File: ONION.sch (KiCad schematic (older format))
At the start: 11 parts

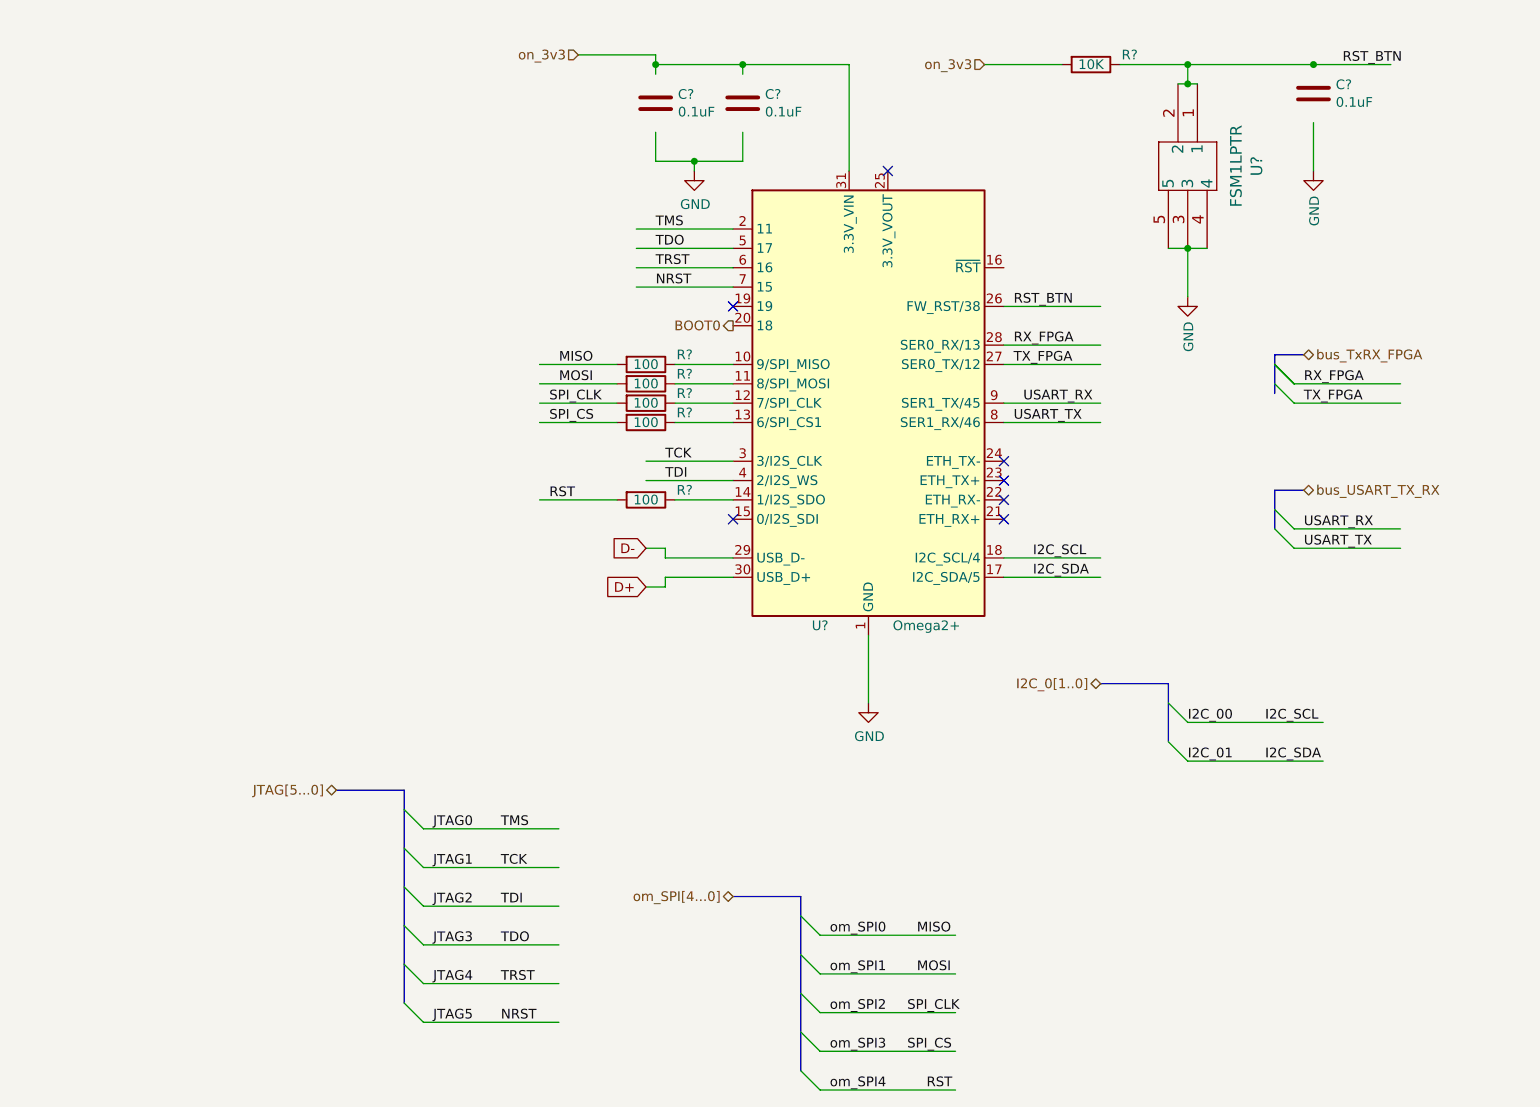
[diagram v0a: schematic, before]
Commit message: asignacion pines de control
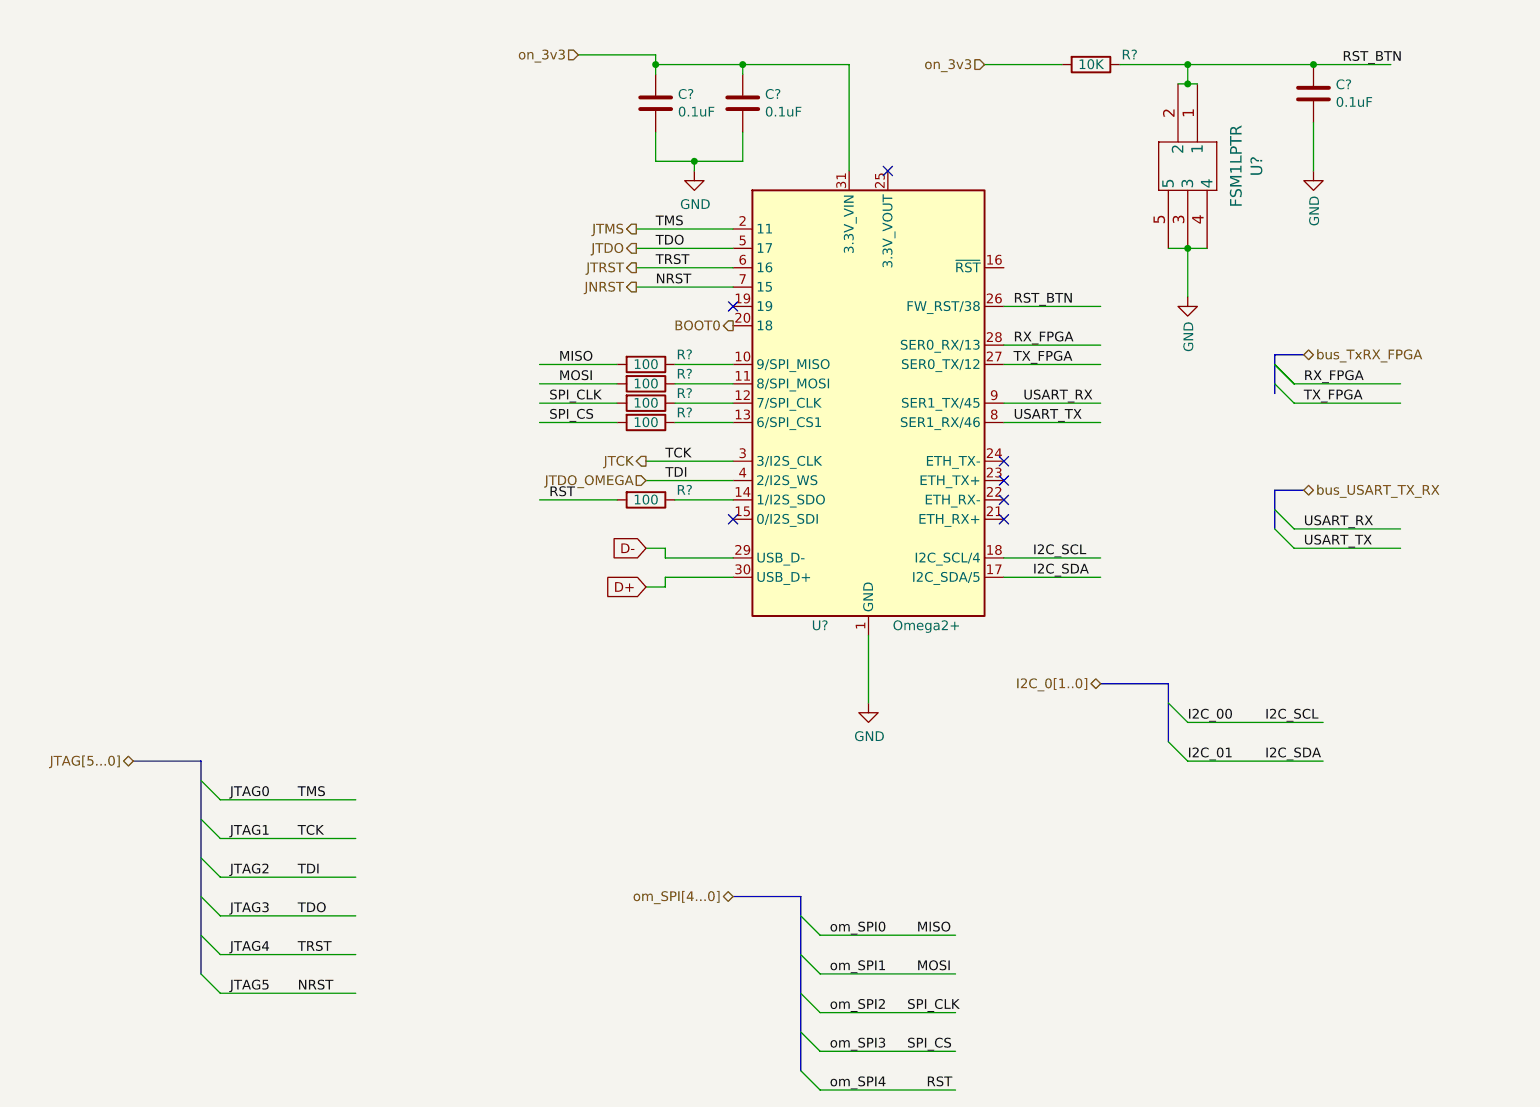
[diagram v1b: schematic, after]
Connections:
- net labels added: JNRST, JTCK, JTDO, JTDO_OMEGA, JTMS, JTRST
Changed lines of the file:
@@
 $Descr A4 11693 8268
 encoding utf-8
-Sheet 4 5
+Sheet 4 6
 Title ""
 Date ""
@@
 $Comp
 L Device:C C?
-U 0 1 5D451473
+U 1 1 5D451473
 P 4350 1700
 AR Path="/5CD05F2F/5D451473" Ref="C?"  Part="0"
@@
 F 2 "Capacitor_SMD:C_0603_1608Metric_Pad1.05x0.95mm_HandSolder" H 4388 1550 50  0001 C CNN
 F 3 "" H 4350 1700 50  0001 C CNN
-	0    4350 1700
+	1    4350 1700
 	1    0    0    -1
 $EndComp
@@
 $Comp
 L Device:C C?
-U 0 1 5D44FAD3
+U 1 1 5D44FAD3
 P 3900 1700
 AR Path="/5CD05F2F/5D44FAD3" Ref="C?"  Part="0"
@@
 F 2 "Capacitor_SMD:C_0603_1608Metric_Pad1.05x0.95mm_HandSolder" H 3938 1550 50  0001 C CNN
 F 3 "" H 3900 1700 50  0001 C CNN
-	0    3900 1700
+	1    3900 1700
 	1    0    0    -1
 $EndComp
@@
 USART_TX
 Wire Bus Line
-	2250 5250 2600 5250
-Entry Wire Line
-	2600 5350 2700 5450
-Entry Wire Line
-	2600 5550 2700 5650
-Entry Wire Line
-	2600 5750 2700 5850
-Entry Wire Line
-	2600 5950 2700 6050
-Entry Wire Line
-	2600 6150 2700 6250
-Entry Wire Line
-	2600 6350 2700 6450
-Wire Wire Line
-	2700 5450 3400 5450
-Wire Wire Line
-	2700 5650 3400 5650
-Wire Wire Line
-	2700 5850 3400 5850
-Wire Wire Line
-	2700 6050 3400 6050
-Wire Wire Line
-	2700 6250 3400 6250
-Wire Wire Line
-	2700 6450 3400 6450
-Wire Bus Line
 	6200 4700 6550 4700
 Entry Wire Line
@@
 Wire Wire Line
 	4750 6800 5450 6800
-Text Label 2750 5450 0    50   ~ 0
-JTAG0
-Text Label 2750 5650 0    50   ~ 0
-JTAG1
-Text Label 2750 5850 0    50   ~ 0
-JTAG2
-Text Label 2750 6050 0    50   ~ 0
-JTAG3
-Text Label 2750 6250 0    50   ~ 0
-JTAG4
-Text Label 2750 6450 0    50   ~ 0
-JTAG5
-Text HLabel 2250 5250 0    50   BiDi ~ 0
-JTAG[5...0]
-Text Label 3100 5450 0    50   ~ 0
-TMS
-Text Label 3100 5650 0    50   ~ 0
-TCK
-Text Label 3100 5850 0    50   ~ 0
-TDI
-Text Label 3100 6050 0    50   ~ 0
-TDO
-Text Label 3100 6250 0    50   ~ 0
-TRST
-Text Label 3100 6450 0    50   ~ 0
-NRST
 Wire Wire Line
 	4300 2350 3800 2350
@@
 Text Label 5300 6800 0    50   ~ 0
 RST
-Text HLabel 4300 5800 0    50   BiDi ~ 0
-om_SPI[4...0]
 $Comp
 L BAT2032:R R?
@@
 $Comp
 L Device:C C?
-U 0 1 5CD5AB36
+U 1 1 5CD5AB36
 P 7300 1650
 AR Path="/5CD05F2F/5CD5AB36" Ref="C?"  Part="0"
@@
 F 2 "Capacitor_SMD:C_0603_1608Metric_Pad1.05x0.95mm_HandSolder" H 7338 1500 50  0001 C CNN
 F 3 "" H 7300 1650 50  0001 C CNN
-	0    7300 1650
+	1    7300 1650
 	1    0    0    -1
 $EndComp
@@
 	0    1    1    0
 $EndComp
+Text HLabel 4300 5800 0    50   BiDi ~ 0
+om_SPI[4...0]
+Text Label 2050 6300 0    50   ~ 0
+NRST
+Text Label 2050 6100 0    50   ~ 0
+TRST
+Text Label 2050 5900 0    50   ~ 0
+TDO
+Text Label 2050 5700 0    50   ~ 0
+TDI
+Text Label 2050 5500 0    50   ~ 0
+TCK
+Text Label 2050 5300 0    50   ~ 0
+TMS
+Text HLabel 1200 5100 0    50   BiDi ~ 0
+JTAG[5...0]
+Text Label 1700 6300 0    50   ~ 0
+JTAG5
+Text Label 1700 6100 0    50   ~ 0
+JTAG4
+Text Label 1700 5900 0    50   ~ 0
+JTAG3
+Text Label 1700 5700 0    50   ~ 0
+JTAG2
+Text Label 1700 5500 0    50   ~ 0
+JTAG1
+Text Label 1700 5300 0    50   ~ 0
+JTAG0
+Wire Wire Line
+	1650 6300 2350 6300
+Wire Wire Line
+	1650 6100 2350 6100
+Wire Wire Line
+	1650 5900 2350 5900
+Wire Wire Line
+	1650 5700 2350 5700
+Wire Wire Line
+	1650 5500 2350 5500
+Wire Wire Line
+	1650 5300 2350 5300
+Entry Wire Line
+	1550 6200 1650 6300
+Entry Wire Line
+	1550 6000 1650 6100
+Entry Wire Line
+	1550 5800 1650 5900
+Entry Wire Line
+	1550 5600 1650 5700
+Entry Wire Line
+	1550 5400 1650 5500
+Entry Wire Line
+	1550 5200 1650 5300
+Wire Bus Line
+	1200 5100 1550 5100
+Text HLabel 3800 2450 0    50   Output ~ 0
+JTDO
+Text HLabel 3800 2350 0    50   Output ~ 0
+JTMS
+Text HLabel 3800 2550 0    50   Output ~ 0
+JTRST
+Text HLabel 3800 2650 0    50   Output ~ 0
+JNRST
+Text HLabel 3850 3550 0    50   Output ~ 0
+JTCK
+Text HLabel 3850 3650 0    50   Input ~ 0
+JTDO_OMEGA
 Wire Bus Line
 	6550 4700 6550 5000
@@
 	4650 5800 4650 6700
 Wire Bus Line
-	2600 5250 2600 6350
+	1550 5100 1550 6200
 $EndSCHEMATC

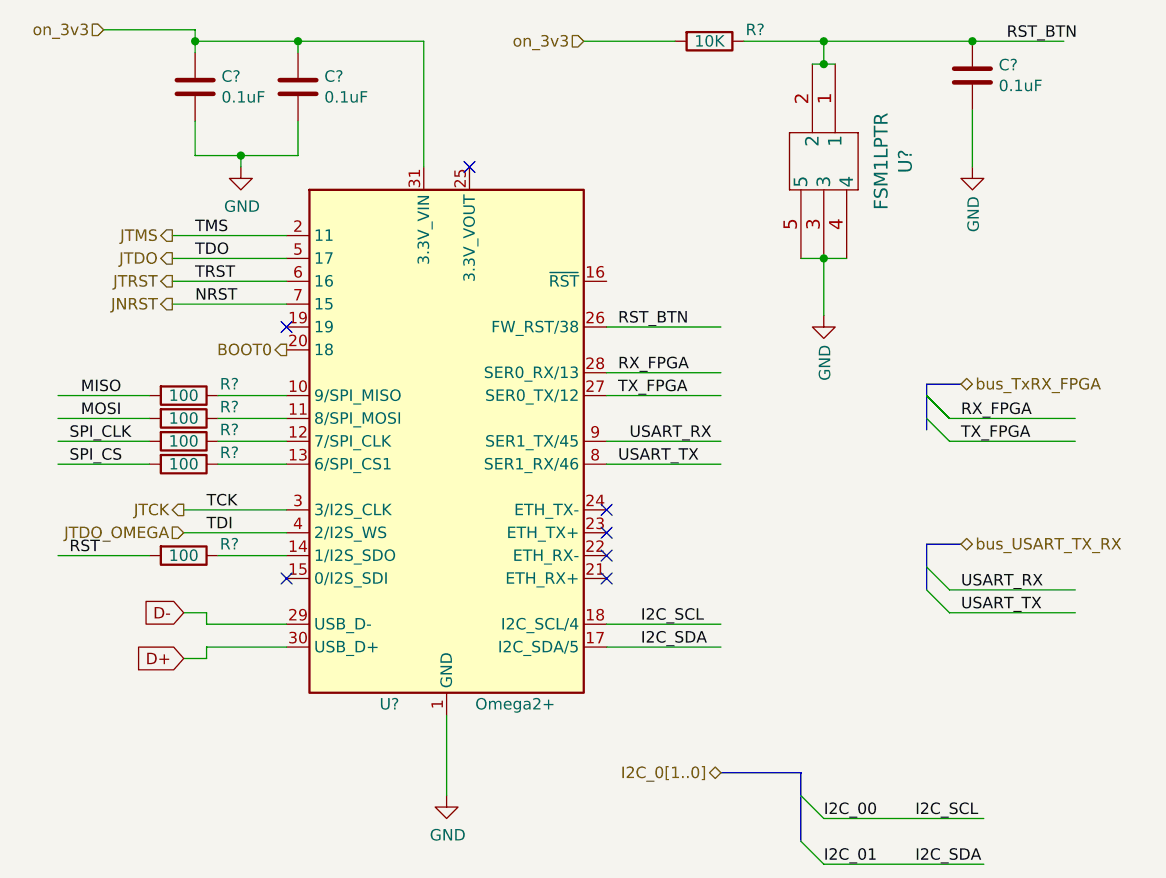
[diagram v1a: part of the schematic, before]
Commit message: asignacion pines de control
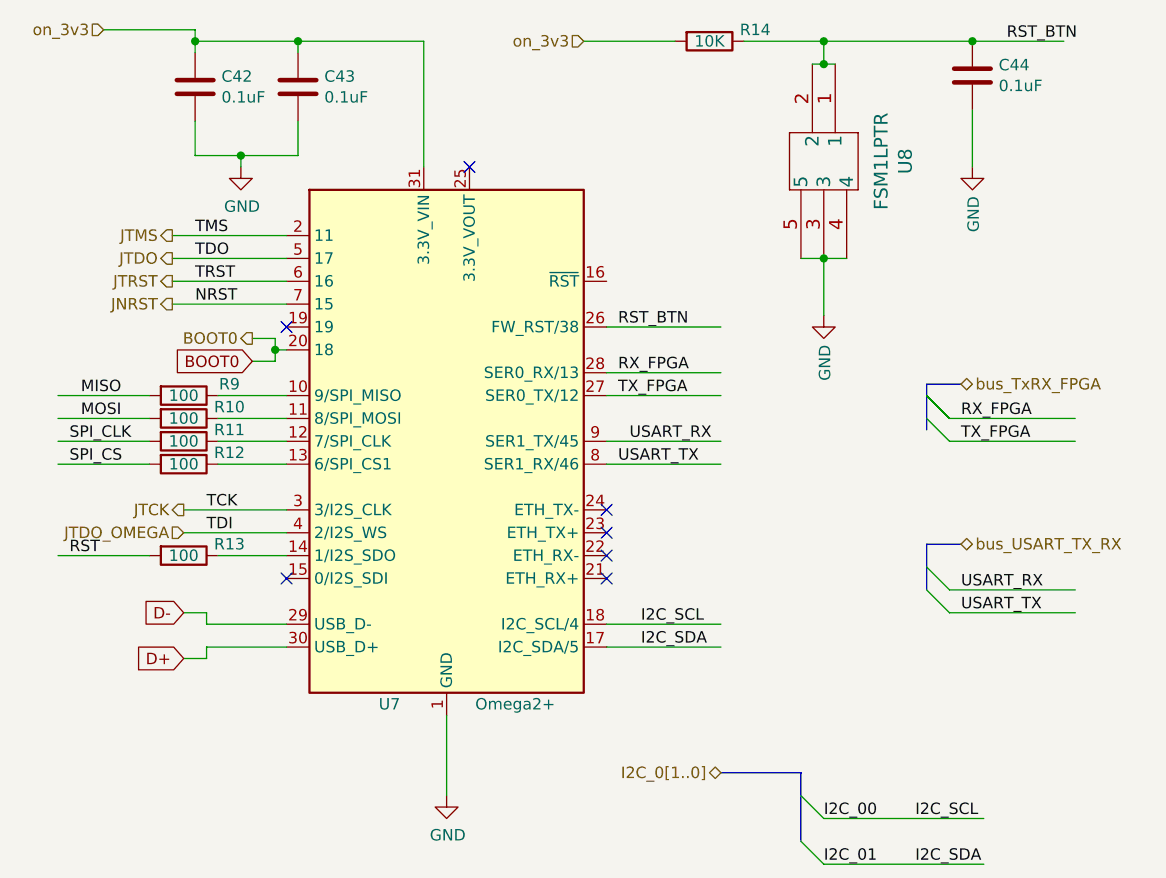
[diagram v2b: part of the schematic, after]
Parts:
- gave numbers to parts that had none: 11
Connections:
- wire segments 70 -> 75
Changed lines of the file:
@@
 $EndDescr
 $Comp
-L power:GND #PWR?
+L power:GND #PWR0143
 U 1 1 5D428107
 P 5000 4800
-F 0 "#PWR?" H 5000 4550 50  0001 C CNN
+F 0 "#PWR0143" H 5000 4550 50  0001 C CNN
 F 1 "GND" H 5005 4627 50  0000 C CNN
 F 2 "" H 5000 4800 50  0001 C CNN
@@
 P 4350 1700
 AR Path="/5CD05F2F/5D451473" Ref="C?"  Part="0"
-AR Path="/5D3DE78E/5D451473" Ref="C?"  Part="0"
-F 0 "C?" H 4465 1746 50  0000 L CNN
+AR Path="/5D3DE78E/5D451473" Ref="C43"  Part="1"
+F 0 "C43" H 4465 1746 50  0000 L CNN
 F 1 "0.1uF" H 4465 1655 50  0000 L CNN
 F 2 "Capacitor_SMD:C_0603_1608Metric_Pad1.05x0.95mm_HandSolder" H 4388 1550 50  0001 C CNN
@@
 	4350 2000 4100 2000
 $Comp
-L power:GND #PWR?
+L power:GND #PWR0144
 U 1 1 5D454107
 P 4100 2050
-F 0 "#PWR?" H 4100 1800 50  0001 C CNN
+F 0 "#PWR0144" H 4100 1800 50  0001 C CNN
 F 1 "GND" H 4105 1877 50  0000 C CNN
 F 2 "" H 4100 2050 50  0001 C CNN
@@
 P 3900 1700
 AR Path="/5CD05F2F/5D44FAD3" Ref="C?"  Part="0"
-AR Path="/5D3DE78E/5D44FAD3" Ref="C?"  Part="0"
-F 0 "C?" H 4015 1746 50  0000 L CNN
+AR Path="/5D3DE78E/5D44FAD3" Ref="C42"  Part="1"
+F 0 "C42" H 4015 1746 50  0000 L CNN
 F 1 "0.1uF" H 4015 1655 50  0000 L CNN
 F 2 "Capacitor_SMD:C_0603_1608Metric_Pad1.05x0.95mm_HandSolder" H 3938 1550 50  0001 C CNN
@@
 NoConn ~ 5700 3850
 $Comp
-L MCU_Module:Omega2+ U?
+L MCU_Module:Omega2+ U7
 U 1 1 5D3DE9E1
 P 5000 3250
-F 0 "U?" H 4750 2100 50  0000 C CNN
+F 0 "U7" H 4750 2100 50  0000 C CNN
 F 1 "Omega2+" H 5300 2100 50  0000 C CNN
 F 2 "Module:Onion_Omega2+" H 5000 1750 50  0001 C CNN
@@
 RST
 $Comp
-L BAT2032:R R?
+L BAT2032:R R9
 U 1 1 5CD91C3B
 P 3850 3050
-F 0 "R?" V 3800 3250 50  0000 C CNN
+F 0 "R9" V 3800 3250 50  0000 C CNN
 F 1 "100" V 3850 3050 50  0000 C CNN
 F 2 "Resistor_SMD:R_0603_1608Metric_Pad1.05x0.95mm_HandSolder" V 3780 3050 50  0001 C CNN
@@
 $EndComp
 $Comp
-L BAT2032:R R?
+L BAT2032:R R10
 U 1 1 5CD95E75
 P 3850 3150
-F 0 "R?" V 3800 3350 50  0000 C CNN
+F 0 "R10" V 3800 3350 50  0000 C CNN
 F 1 "100" V 3850 3150 50  0000 C CNN
 F 2 "Resistor_SMD:R_0603_1608Metric_Pad1.05x0.95mm_HandSolder" V 3780 3150 50  0001 C CNN
@@
 $EndComp
 $Comp
-L BAT2032:R R?
+L BAT2032:R R11
 U 1 1 5CD970C9
 P 3850 3250
-F 0 "R?" V 3800 3450 50  0000 C CNN
+F 0 "R11" V 3800 3450 50  0000 C CNN
 F 1 "100" V 3850 3250 50  0000 C CNN
 F 2 "Resistor_SMD:R_0603_1608Metric_Pad1.05x0.95mm_HandSolder" V 3780 3250 50  0001 C CNN
@@
 $EndComp
 $Comp
-L BAT2032:R R?
+L BAT2032:R R12
 U 1 1 5CD983F0
 P 3850 3350
-F 0 "R?" V 3800 3550 50  0000 C CNN
+F 0 "R12" V 3800 3550 50  0000 C CNN
 F 1 "100" V 3850 3350 50  0000 C CNN
 F 2 "Resistor_SMD:R_0603_1608Metric_Pad1.05x0.95mm_HandSolder" V 3780 3350 50  0001 C CNN
@@
 SPI_CS
 $Comp
-L BAT2032:R R?
+L BAT2032:R R13
 U 1 1 5CD3D226
 P 3850 3750
-F 0 "R?" V 3800 3950 50  0000 C CNN
+F 0 "R13" V 3800 3950 50  0000 C CNN
 F 1 "100" V 3850 3750 50  0000 C CNN
 F 2 "Resistor_SMD:R_0603_1608Metric_Pad1.05x0.95mm_HandSolder" V 3780 3750 50  0001 C CNN
@@
 Text Label 3350 3750 0    50   ~ 0
 RST
-Text HLabel 4300 2850 0    50   Output ~ 0
+Text HLabel 4150 2800 0    50   Output ~ 0
 BOOT0
 $Comp
-L power:GND #PWR?
+L power:GND #PWR0145
 U 1 1 5CD47976
 P 6650 2700
-F 0 "#PWR?" H 6650 2450 50  0001 C CNN
+F 0 "#PWR0145" H 6650 2450 50  0001 C CNN
 F 1 "GND" V 6655 2572 50  0000 R CNN
 F 2 "" H 6650 2700 50  0001 C CNN
@@
 	7300 2050 7300 1800
 $Comp
-L power:GND #PWR?
+L power:GND #PWR0146
 U 1 1 5CD5D462
 P 7300 2050
-F 0 "#PWR?" H 7300 1800 50  0001 C CNN
+F 0 "#PWR0146" H 7300 1800 50  0001 C CNN
 F 1 "GND" V 7305 1922 50  0000 R CNN
 F 2 "" H 7300 2050 50  0001 C CNN
@@
 P 7300 1650
 AR Path="/5CD05F2F/5CD5AB36" Ref="C?"  Part="0"
-AR Path="/5D3DE78E/5CD5AB36" Ref="C?"  Part="0"
-F 0 "C?" H 7415 1696 50  0000 L CNN
+AR Path="/5D3DE78E/5CD5AB36" Ref="C44"  Part="1"
+F 0 "C44" H 7415 1696 50  0000 L CNN
 F 1 "0.1uF" H 7415 1605 50  0000 L CNN
 F 2 "Capacitor_SMD:C_0603_1608Metric_Pad1.05x0.95mm_HandSolder" H 7338 1500 50  0001 C CNN
@@
 $EndComp
 $Comp
-L BAT2032:R R?
+L BAT2032:R R14
 U 1 1 5CD54029
 P 6150 1500
-F 0 "R?" V 6100 1700 50  0000 C CNN
+F 0 "R14" V 6100 1700 50  0000 C CNN
 F 1 "10K" V 6150 1500 50  0000 C CNN
 F 2 "Resistor_SMD:R_0603_1608Metric_Pad1.05x0.95mm_HandSolder" V 6080 1500 50  0001 C CNN
@@
 	6750 2450 6650 2450
 $Comp
-L FSM1LPTR:FSM1LPTR U?
+L FSM1LPTR:FSM1LPTR U8
 U 1 1 5D472323
 P 6700 2000
-F 0 "U?" H 6725 2307 60  0000 C CNN
+F 0 "U8" H 6725 2307 60  0000 C CNN
 F 1 "FSM1LPTR" H 6725 2201 60  0000 C CNN
 F 2 "SWITCH_FSM1LPA" H 6700 2150 60  0001 C CNN
@@
 Text HLabel 3850 3650 0    50   Input ~ 0
 JTDO_OMEGA
+Text GLabel 4150 2900 0    50   Input ~ 0
+BOOT0
+Wire Wire Line
+	4300 2850 4250 2850
+Wire Wire Line
+	4250 2850 4250 2800
+Wire Wire Line
+	4250 2800 4150 2800
+Wire Wire Line
+	4150 2900 4250 2900
+Wire Wire Line
+	4250 2900 4250 2850
+Connection ~ 4250 2850
 Wire Bus Line
 	6550 4700 6550 5000

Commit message: retoque casi finales
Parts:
- removed R13: 100, Resistor_SMD:R_0603_1608Metric_Pad1.05x0.95mm_HandSolder, symbol BAT2032:R
- added D14: LED, LED_SMD:LED_0603_1608Metric_Pad1.05x0.95mm_HandSolder, symbol BAT2032:LED
- added J5: Conn_02x06, Connector_PinHeader_2.54mm:PinHeader_2x06_P2.54mm_Vertical, symbol Connector_Generic:Conn_02x06_Counter_Clockwise
- added R17: 600, Resistor_SMD:R_0603_1608Metric_Pad1.05x0.95mm_HandSolder, symbol BAT2032:R
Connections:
- net labels added: +5VD, I2C_0[0..1], JTAG[0..5], LED, RX_PIN, TX_PIN, vcc_STM32
- net labels removed: I2C_0[1..0], JTAG[5...0], RST, RX_FPGA, TX_FPGA, bus_TxRX_FPGA, bus_USART_TX_RX, om_SPI0, om_SPI1, om_SPI2, om_SPI3, om_SPI4, om_SPI[4...0]
- wire segments 75 -> 88
- no-connect marks 7 -> 8
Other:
- note added: "RED"
